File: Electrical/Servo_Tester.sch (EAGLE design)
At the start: 10 parts, among them IC1 NE555_DIP

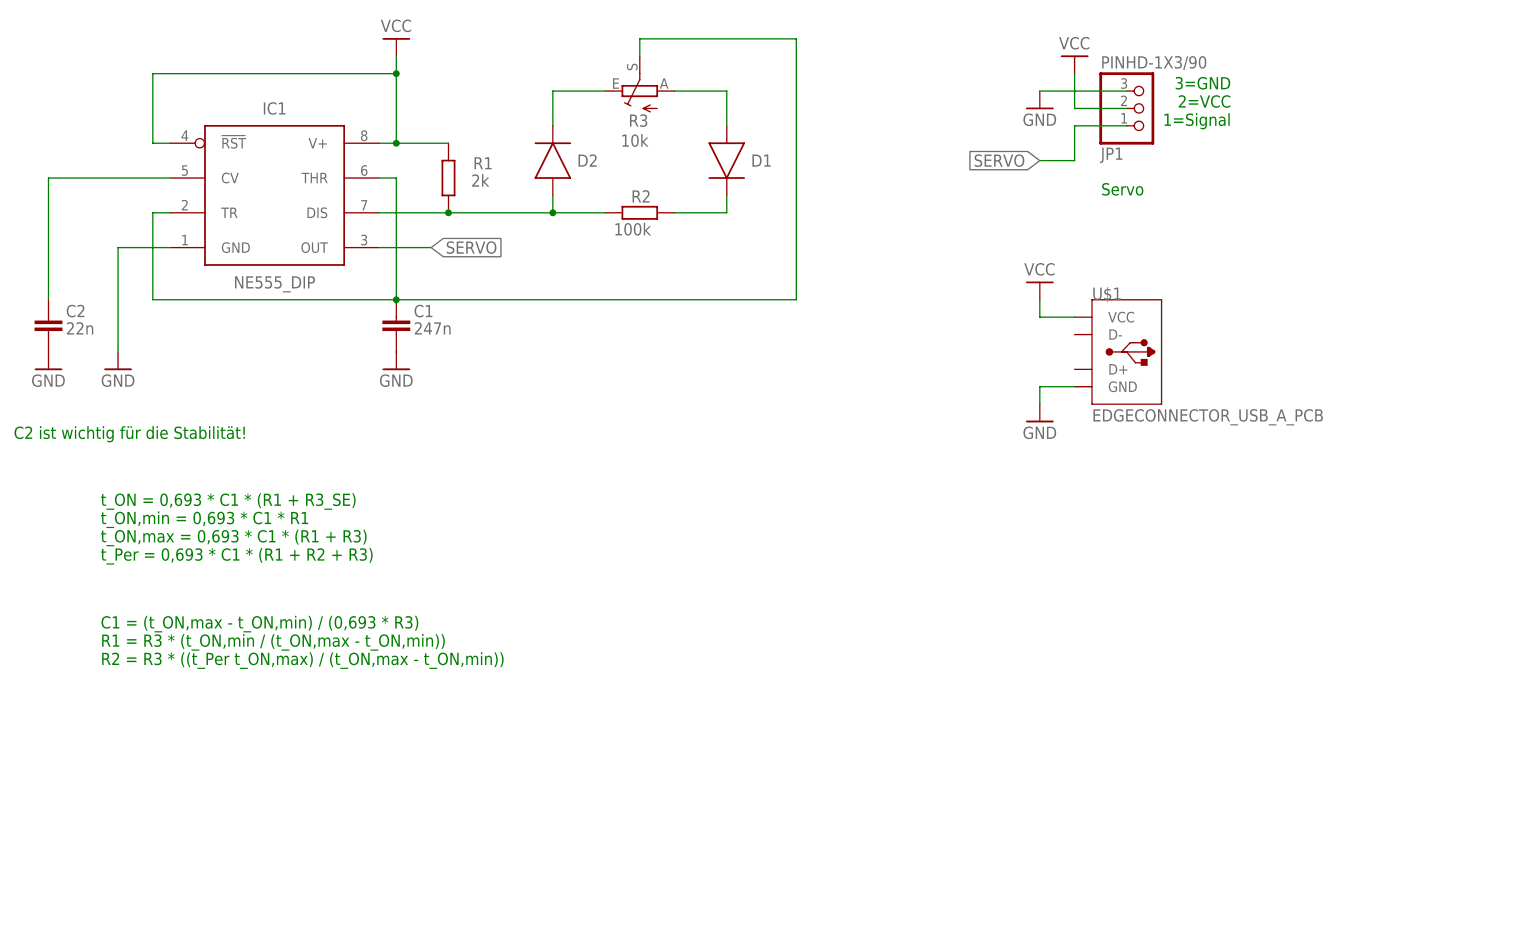
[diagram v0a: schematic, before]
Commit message: Added LED to PCB, slightly adapted some texts
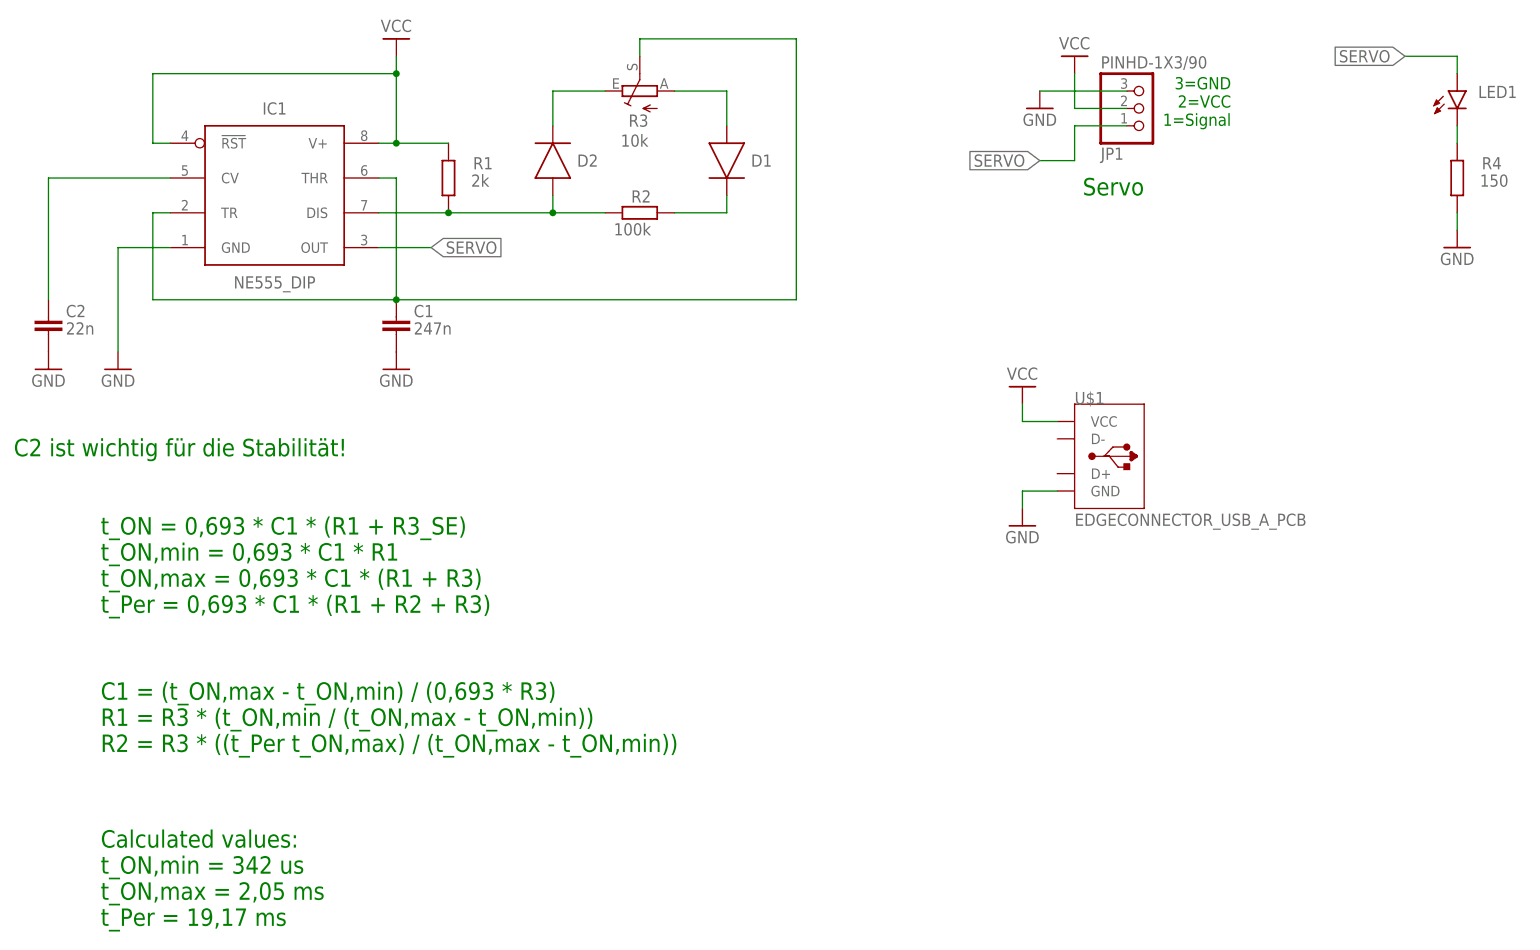
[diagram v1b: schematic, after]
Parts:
- added LED1: (no value), OwnDevices:LEDCHIP-LED0805
- added R4: 150, OwnDevices:R-EU_R0805
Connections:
- new net N$7: LED1.C, R4.2
- net GND: now also R4.1
- net SERVO: now also LED1.A
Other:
- note added: "Calculated values: t_ON,min = 342 us t_ON,max = 2,05 ms t_Per = 19,17 ms"
- moved on the sheet: U$1
